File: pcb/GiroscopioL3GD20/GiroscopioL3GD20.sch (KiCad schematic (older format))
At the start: 22 parts, among them J1 Conn_01x09, Q1 BSS138, Q2 BSS138, U1 MIC5225-3.3YM5, U2 L3GD20H

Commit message: Se realizan correcciones
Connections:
- no-connect marks 4 -> 3
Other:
- note added: "Gyroscope & level shifters"
- note removed: "Gyroscope"
- note removed: "Power level converter"
- moved on the sheet: J1

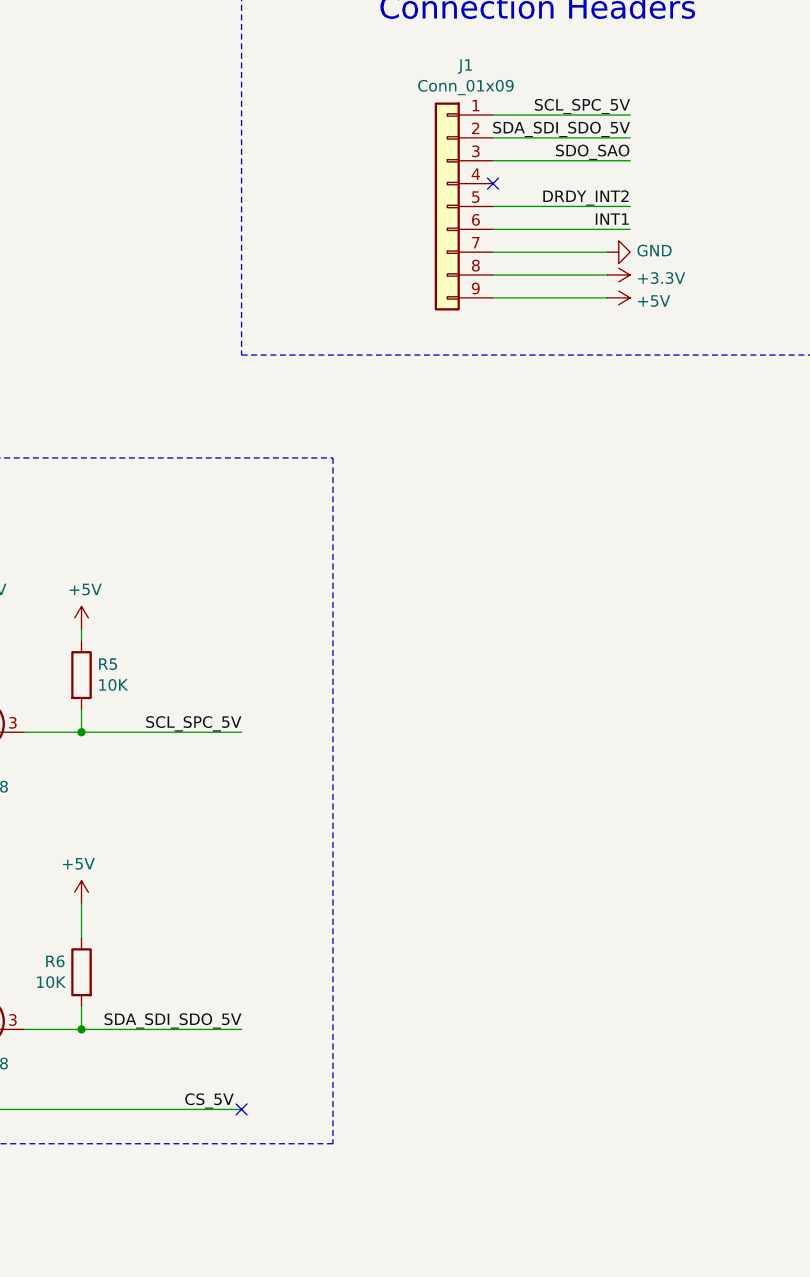
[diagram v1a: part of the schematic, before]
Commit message: Se agrega Placement, borde de placa, notas de PCB, cotas y otros.
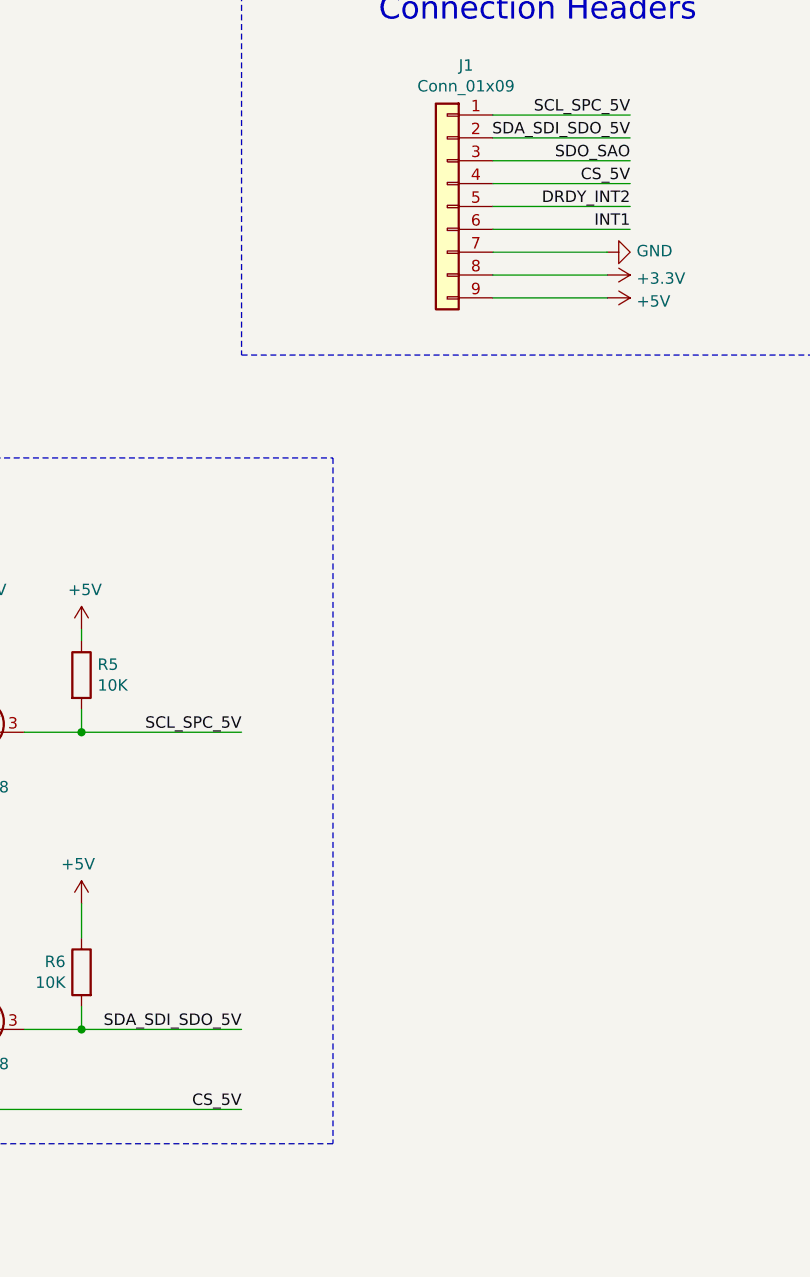
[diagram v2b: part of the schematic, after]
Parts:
- C1, C2, C3, C4: footprint (none) -> Capacitor_SMD:C_0805_2012Metric_Pad1.18x1.45mm_HandSolder
- FID1, FID2: footprint (none) -> Fiducial:Fiducial_1mm_Mask2mm
- H1, H2, H3, H4: footprint (none) -> MountingHole:MountingHole_2.5mm_Pad_TopBottom
- J1: footprint (none) -> Connector_PinHeader_2.54mm:PinHeader_1x09_P2.54mm_Vertical
- R1, R2, R3, R4, R5, R6: footprint (none) -> Resistor_SMD:R_0805_2012Metric_Pad1.20x1.40mm_HandSolder
- U2: footprint (none) -> Package_LGA:LGA-16_3x3mm_P0.5mm
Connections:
- net CS_5V: now also J1.4 (Pin_4)
- no-connect marks 3 -> 1

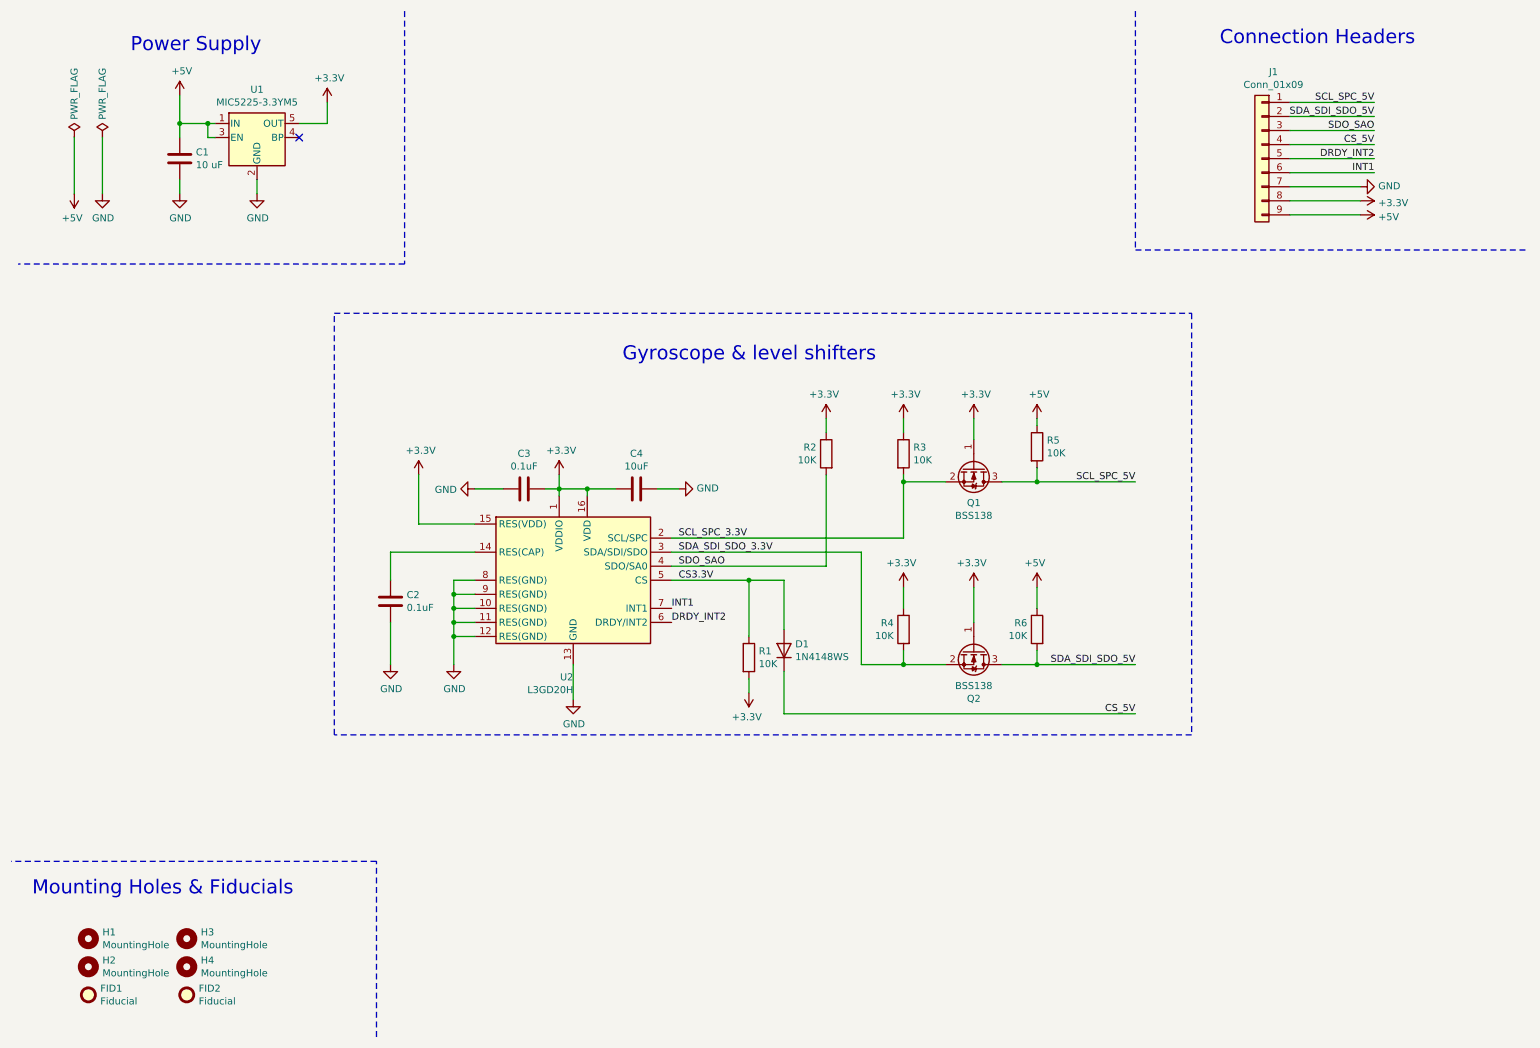
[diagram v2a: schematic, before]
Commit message: Correcciones del esquematico y ruteo del PCB
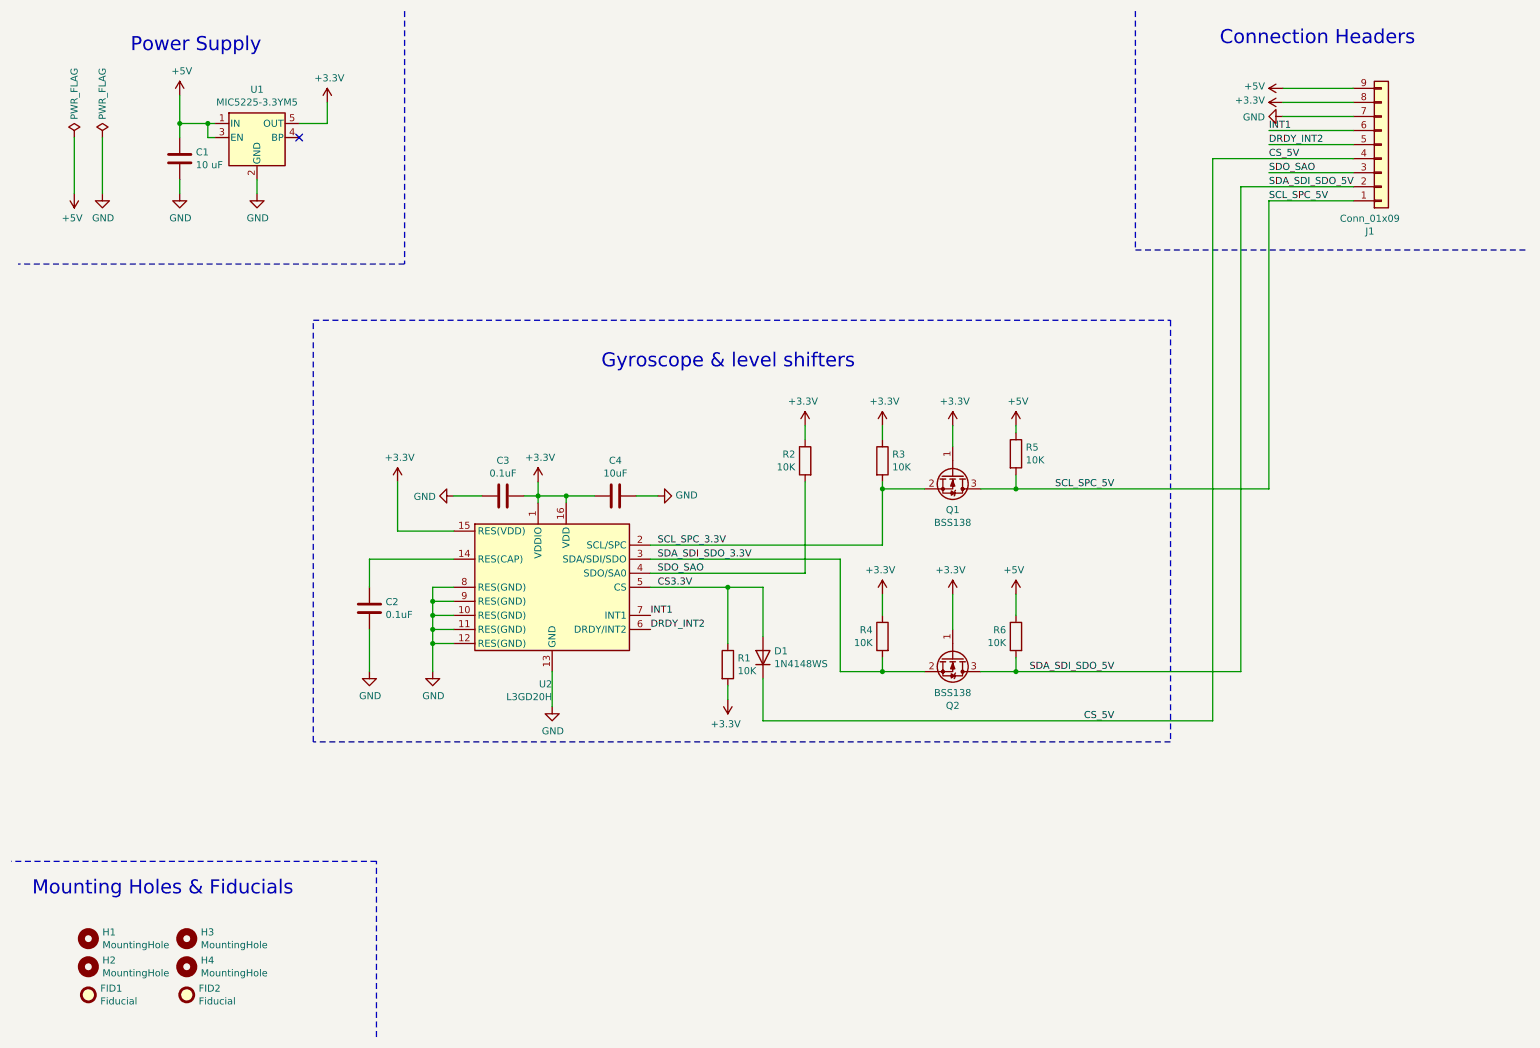
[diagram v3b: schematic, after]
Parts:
- Q1: Digi-Key PN (none) -> BSS138-DIE-ND
- Q2: Digi-Key PN (none) -> BSS138TR-ND
- U1: Digi-Key PN (none) -> 576-2980-2-ND
- U2: Digi-Key PN (none) -> 497-13931-2-ND
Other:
- moved on the sheet: C2, C3, C4, D1, J1, Q1, Q2, R1, R2, R3, R4, R5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

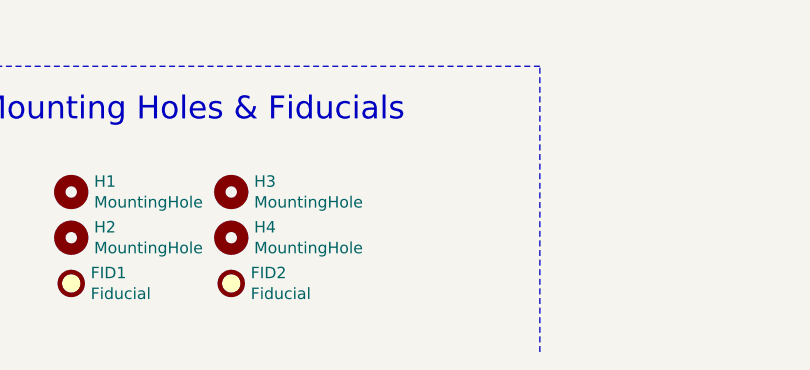
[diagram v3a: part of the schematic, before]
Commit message: Correcciones. Se agrega Fiducial. Se corrigen posiciones de serigrafias.
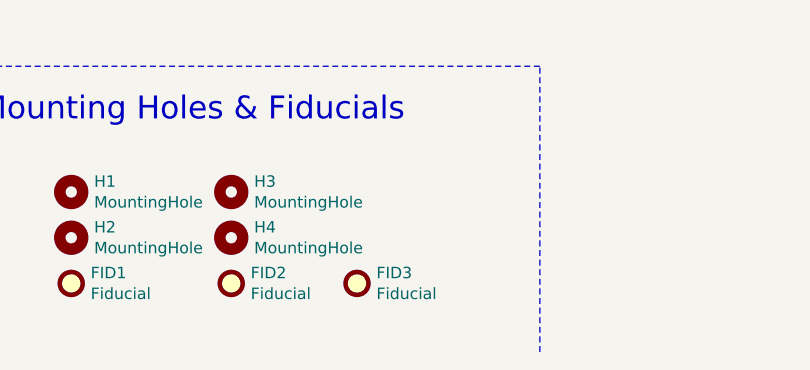
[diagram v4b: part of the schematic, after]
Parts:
- added FID3: Fiducial, Fiducial:Fiducial_1mm_Mask2mm, symbol Mechanical:Fiducial
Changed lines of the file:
@@
 Wire Wire Line
 	7600 5200 9200 5200
+$Comp
+L Mechanical:Fiducial FID3
+U 1 1 611A7A0A
+P 2250 7500
+F 0 "FID3" H 2335 7546 50  0000 L CNN
+F 1 "Fiducial" H 2335 7455 50  0000 L CNN
+F 2 "Fiducial:Fiducial_1mm_Mask2mm" H 2250 7500 50  0001 C CNN
+F 3 "~" H 2250 7500 50  0001 C CNN
+	1    2250 7500
+	1    0    0    -1
+$EndComp
 $EndSCHEMATC
